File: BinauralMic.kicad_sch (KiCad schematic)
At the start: 65 parts, among them IC1 PCM2903CDBR, J1 156-4218-E, J2 USB_C_Receptacle_USB2.0_16P, J3 Conn_01x02_Pin, J4 Conn_01x02_Pin, SW1 SW_Push, SW2 SW_Push, SW3 SW_Push, U1 74LVC1G08, U2 MIC5504-3.3YM5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

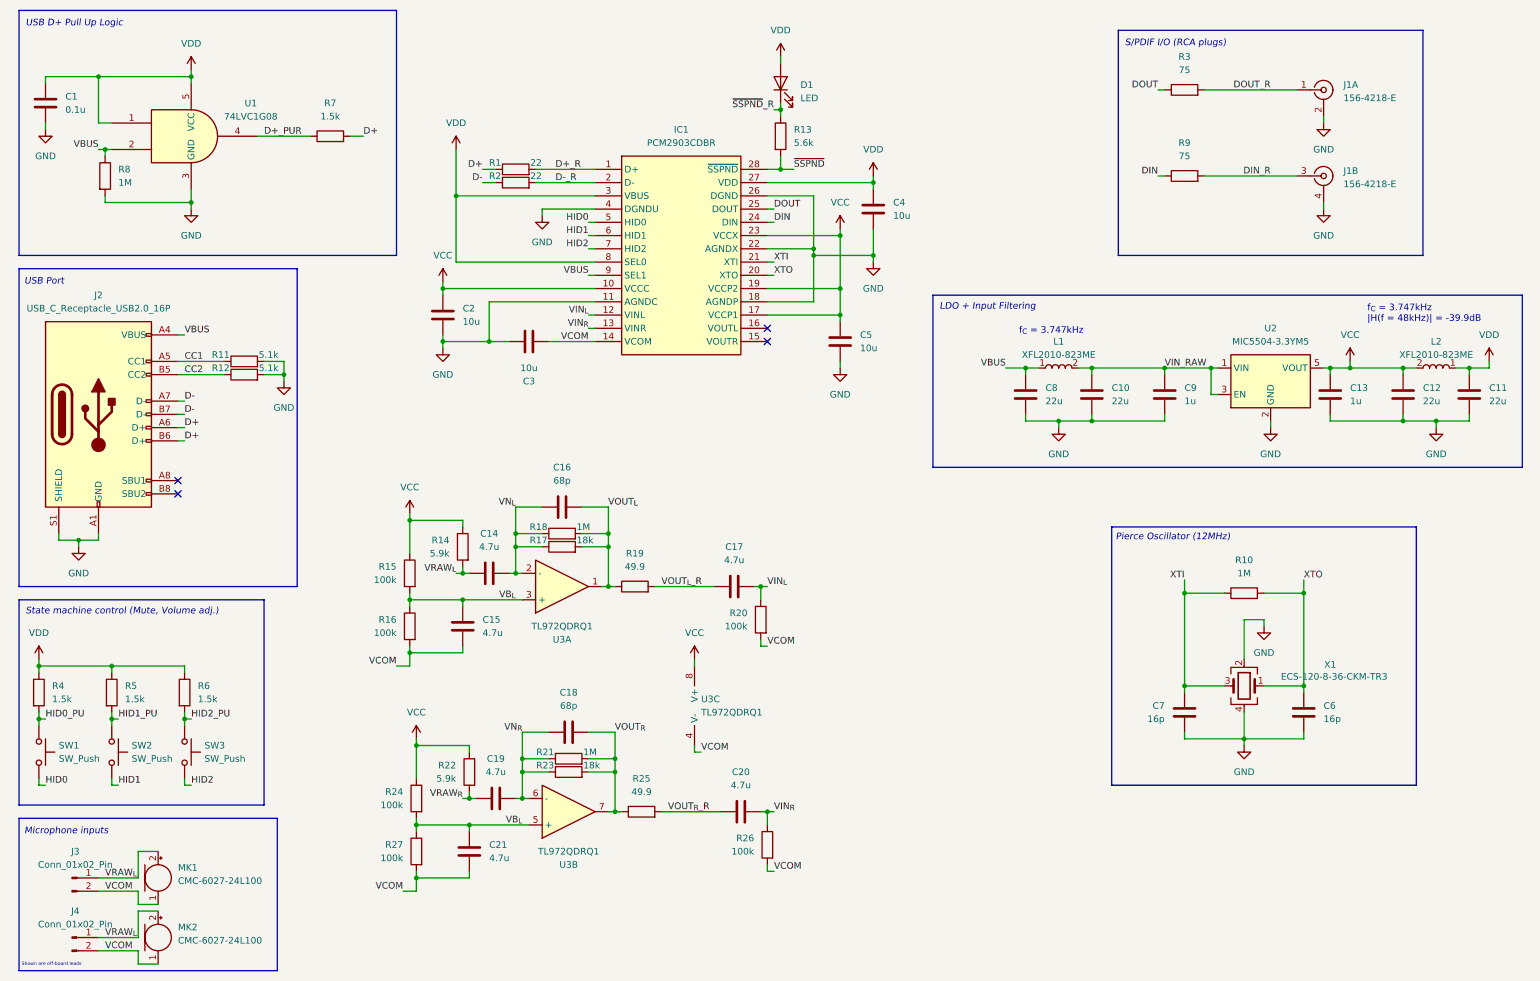
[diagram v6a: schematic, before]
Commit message: Reorganized schematic
Should be much cleaner now
And added a random shunt resistor to measure current coming out of Op Amp (should be ok)
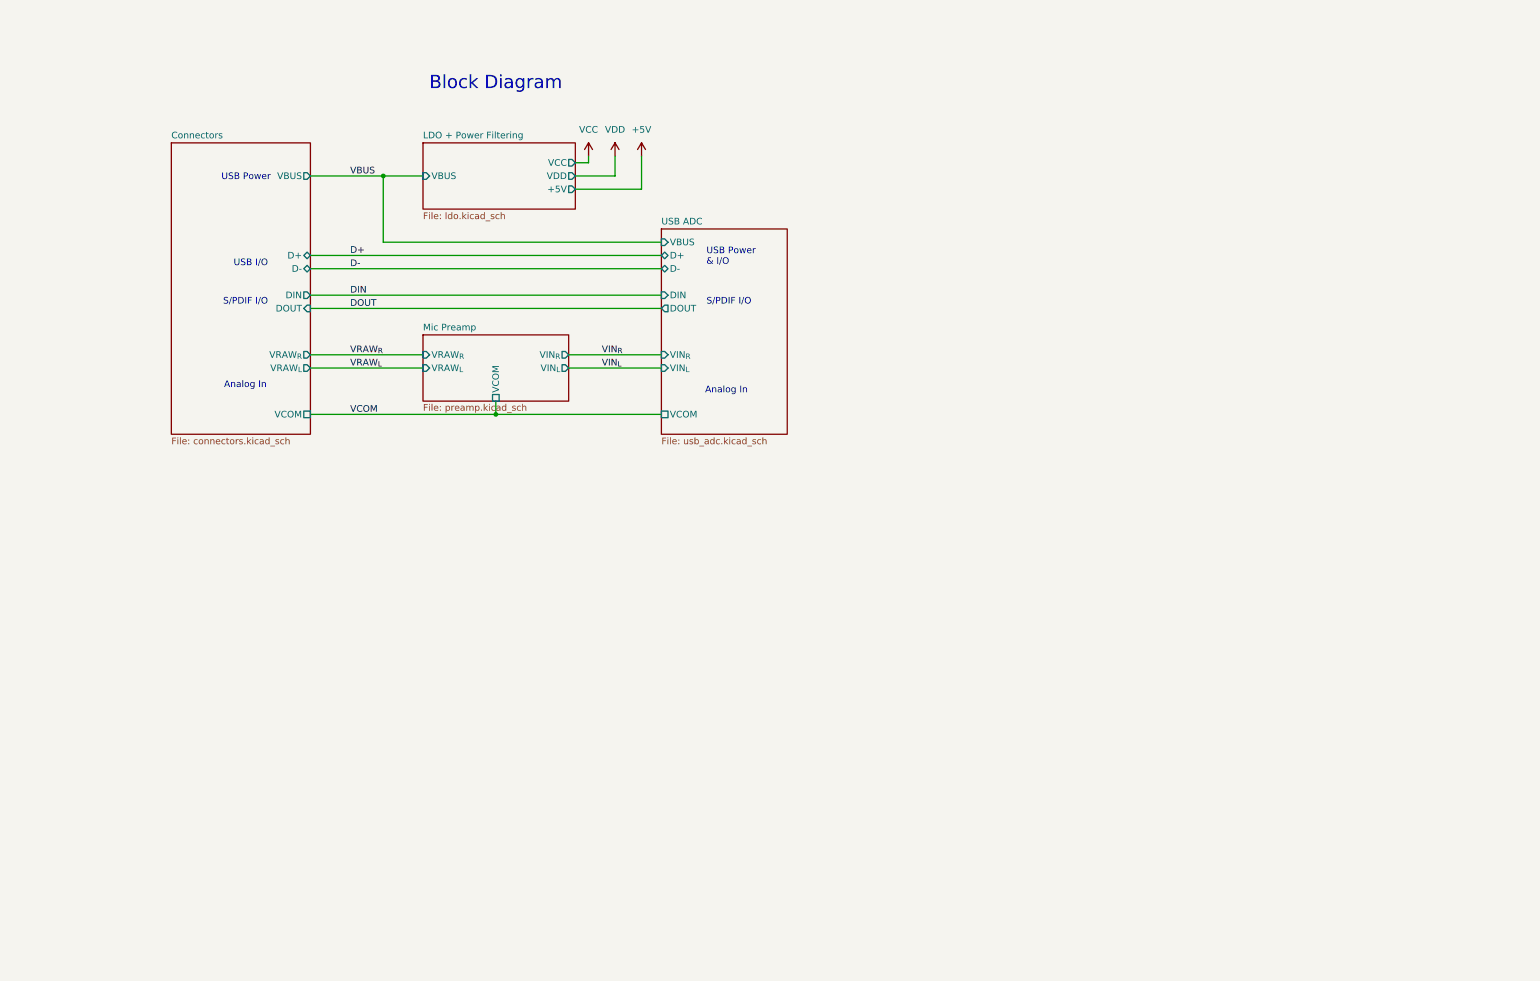
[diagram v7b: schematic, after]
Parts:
- removed C1: 0.1u, symbol Device:C
- removed C10, C11, C12, C8: 22u, symbol Device:C
- removed C13, C9: 1u, symbol Device:C
- removed C14, C15, C17, C19, C20, C21: 4.7u, Capacitor_SMD:C_0603_1608Metric_Pad1.08x0.95mm_HandSolder, symbol Device:C
- removed C16, C18: 68p, Capacitor_SMD:C_0603_1608Metric_Pad1.08x0.95mm_HandSolder, symbol Device:C
- removed C2, C3, C4, C5: 10u, Capacitor_SMD:C_0603_1608Metric_Pad1.08x0.95mm_HandSolder, symbol Device:C
- removed C6, C7: 16p, Capacitor_SMD:C_0603_1608Metric_Pad1.08x0.95mm_HandSolder, symbol Device:C
- removed D1: LED, LED_SMD:LED_0603_1608Metric_Pad1.05x0.95mm_HandSolder, symbol Device:LED
- removed IC1: PCM2903CDBR, binauralmic:SOP65P780X200-28N, symbol binauralmic:PCM2903CDBR
- removed J1: 156-4218-E, binauralmic:1564218E, symbol Connector:Conn_Coaxial_x2_Isolated
- removed J2: USB_C_Receptacle_USB2.0_16P, Connector_USB:USB_C_Receptacle_GCT_USB4105-xx-A_16P_TopMnt_Horizontal, symbol Connector:USB_C_Receptacle_USB2.0_16P
- removed J3, J4: Conn_01x02_Pin, Connector_PinHeader_2.00mm:PinHeader_1x02_P2.00mm_Vertical, symbol Connector:Conn_01x02_Pin
- removed L1, L2: XFL2010-823ME, Inductor_SMD:L_Coilcraft_XFL2010, symbol Device:L
- removed MK1, MK2: CMC-6027-24L100, symbol Device:Microphone
- removed R1, R2: 22, symbol Device:R
- removed R10: 1M, Resistor_SMD:R_0603_1608Metric_Pad0.98x0.95mm_HandSolder, symbol Device:R
- removed R11, R12: 5.1k, symbol Device:R
- removed R13: 5.6k, symbol Device:R
- removed R14, R22: 5.9k, symbol Device:R
- removed R15, R16, R20, R24, R26, R27: 100k, symbol Device:R
- removed R17, R23: 18k, symbol Device:R
- removed R18, R21, R8: 1M, symbol Device:R
- removed R19, R25: 49.9, symbol Device:R
- removed R3, R9: 75, symbol Device:R
- removed R4, R5, R6, R7: 1.5k, symbol Device:R
- removed SW1, SW2, SW3: SW_Push, symbol Switch:SW_Push
- removed U1: 74LVC1G08, Package_TO_SOT_SMD:SOT-23-5_HandSoldering, symbol 74xGxx:74LVC1G08
- removed U2: MIC5504-3.3YM5, Package_TO_SOT_SMD:SOT-23-5_HandSoldering, symbol Regulator_Linear:MIC5504-3.3YM5
- removed U3: TL972QDRQ1, Package_SO:SOIC-8_3.9x4.9mm_P1.27mm, symbol Device:Opamp_Dual
- removed X1: ECS-120-8-36-CKM-TR3, binauralmic:ECS120836CKMTR3, symbol Device:Crystal_GND24
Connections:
- no-connect marks 4 -> 0
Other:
- added sheet Connectors (connectors.kicad_sch)
- added sheet LDO + Power Filtering (ldo.kicad_sch)
- added sheet Mic Preamp (preamp.kicad_sch)
- added sheet USB ADC (usb_adc.kicad_sch)
- note added: "Analog In"
- note added: "Block Diagram"
- note added: "S/PDIF I/O"
- note added: "USB I/O"
- note added: "USB Power"
- note added: "USB Power & I/O"
- note removed: "LDO + Input Filtering"
- note removed: "Microphone inputs"
- note removed: "Pierce Oscillator (12MHz)"
- note removed: "S/PDIF I/O (RCA plugs)"
- note removed: "Shown are off-board leads"
- note removed: "State machine control (Mute, Volume adj.)"
- note removed: "USB D+ Pull Up Logic"
- note removed: "USB Port"
- note removed: "f_{C} = 3.747kHz"
- note removed: "f_{C} = 3.747kHz |H(f = 48kHz)| = -39.9dB"

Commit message: Resnap text to grid + add .gitignore
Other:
- title: Binaural Mic -> Binaural Mic (Block Diagram)
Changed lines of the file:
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@@
 	(paper "A5")
 	(title_block
-		(title "Binaural Mic")
-		(date "2024-09-12")
+		(title "Binaural Mic (Block Diagram)")
+		(date "2024-09-15")
 		(rev "1")
 		(company "Tachyon PCBAs")
@@
 	(text "Analog In"
 		(exclude_from_sim no)
-		(at 144.272 85.598 0)
+		(at 144.78 84.455 0)
 		(effects
 			(font
@@
 	(text "USB Power"
 		(exclude_from_sim no)
-		(at 60.96 44.704 0)
+		(at 60.96 44.45 0)
 		(effects
 			(font
@@
 	(text "S/PDIF I/O"
 		(exclude_from_sim no)
-		(at 144.526 68.58 0)
+		(at 144.78 68.58 0)
 		(effects
 			(font
@@
 	(text "USB I/O"
 		(exclude_from_sim no)
-		(at 60.452 61.214 0)
+		(at 60.96 60.96 0)
 		(effects
 			(font
@@
 	(text "USB Power\n& I/O"
 		(exclude_from_sim no)
-		(at 144.526 59.944 0)
+		(at 144.78 60.325 0)
 		(effects
 			(font
@@
 	(text "S/PDIF I/O"
 		(exclude_from_sim no)
-		(at 60.452 68.58 0)
+		(at 60.96 68.58 0)
 		(effects
 			(font
@@
 	(text "Analog In"
 		(exclude_from_sim no)
-		(at 60.198 84.582 0)
-		(effects
-			(font
+		(at 60.96 85.09 0)
+		(effects
+			(font
